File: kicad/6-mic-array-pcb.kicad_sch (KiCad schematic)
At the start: 11 parts, among them J1 USB-C-16P, U1 SF32LB52JUD6, U2 ADAU1977, U3 XC6206P332MR, U4 XC6206P332MR

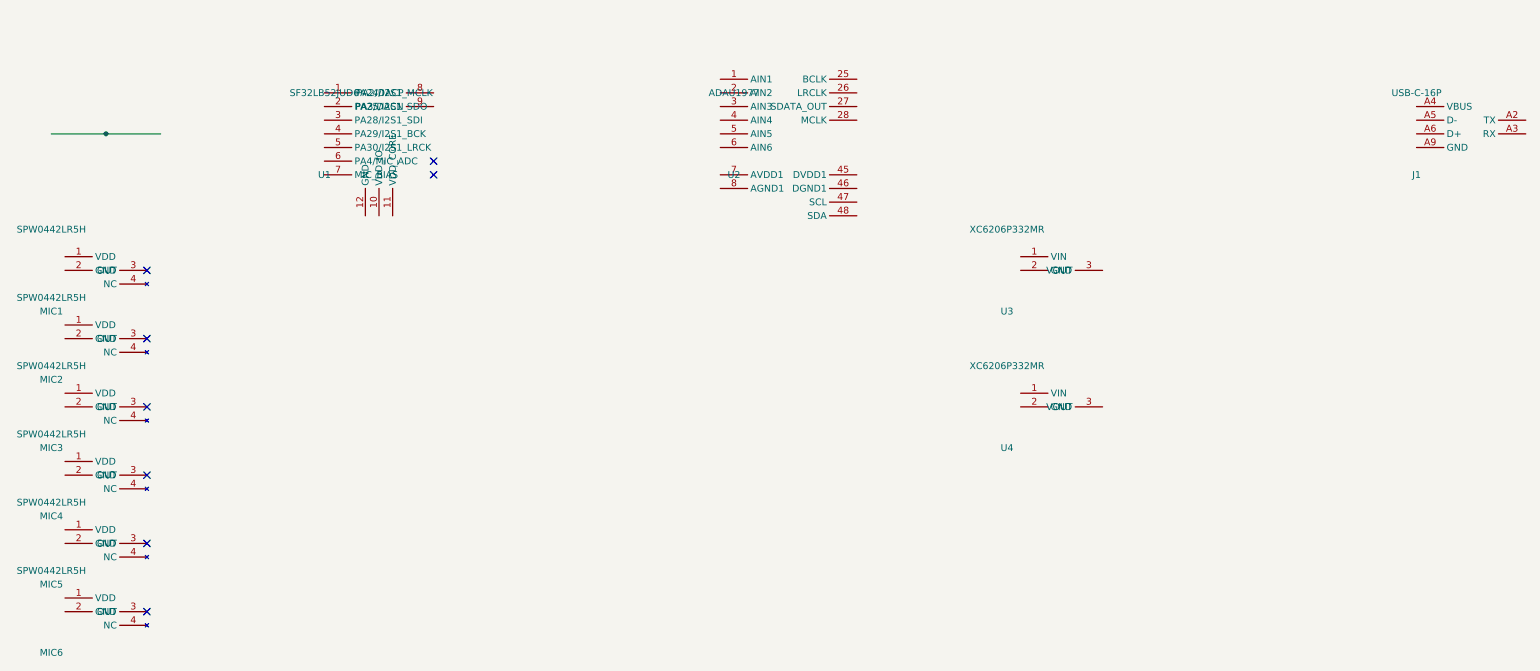
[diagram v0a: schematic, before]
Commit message: feat(common): add pdf
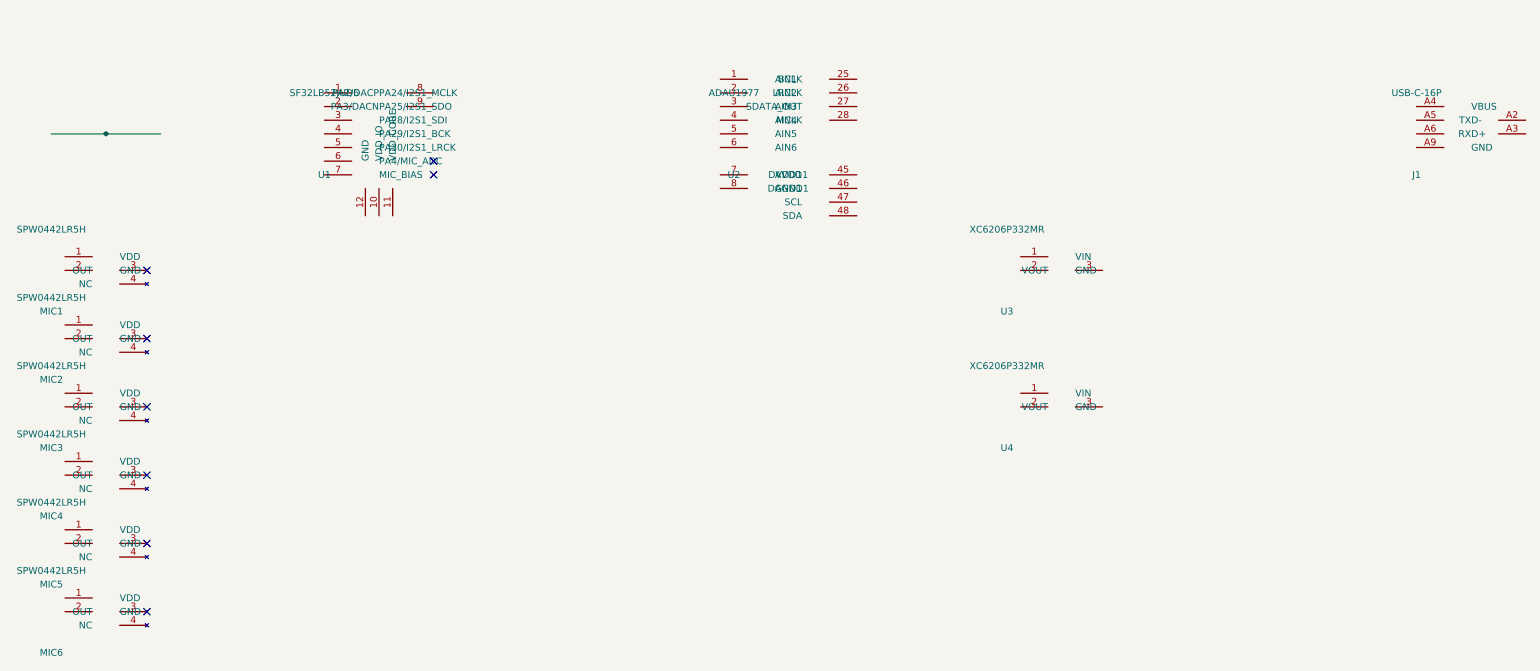
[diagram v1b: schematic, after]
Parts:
- J1: footprint Connector_USB:USB_C_Receptacle_PCB -> Connector_USB:USB_C_Receptacle_Amphenol_12401548E4-2A
- MIC1, MIC2, MIC3, MIC4, MIC5, MIC6: footprint Microphone:MEMS_Mic_SMD_4.72x3.76mm -> Sensor_Audio:Knowles_LGA-6_4.72x3.76mm
- U1: footprint Package_LGA:LGA-56_6x6mm_P0.65mm -> 6-mic-array:SF32LB52JUD6_LGA56
- U3, U4: footprint Package_TO_SOT_SMD:SOT-23 -> Package_TO_SOT_SMD:SOT-23-3

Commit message: feat(common): add pdf
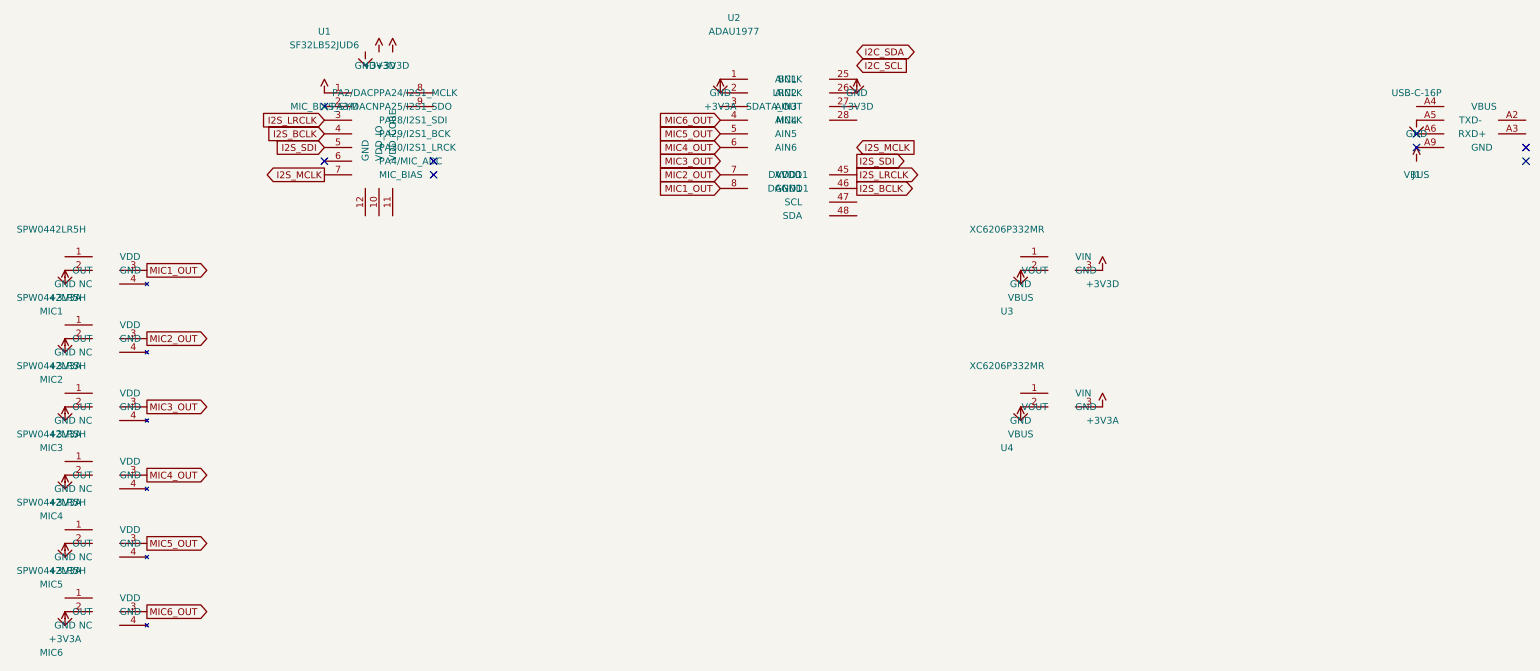
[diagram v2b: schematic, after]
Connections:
- net MIC_BIAS_SYM: now reaches U1.1 (PA24/I2S1_MCLK)
- net I2S_LRCLK: now reaches U1.3 (PA28/I2S1_SDI)
- net I2S_LRCLK: now also U2.45 (DVDD1)
- net I2S_BCLK: now reaches U1.4 (PA29/I2S1_BCK)
- net I2S_BCLK: now also U2.46 (DGND1)
- net I2S_SDI: now reaches U1.5 (PA30/I2S1_LRCK)
- net I2S_MCLK: now reaches U1.7 (MIC_BIAS)
- net GND: now reaches U2.1 (AIN1)
- net GND: now also J1.A5 (D-), MIC1.2 (GND), MIC2.2 (GND), MIC3.2 (GND), MIC4.2 (GND), MIC5.2 (GND), MIC6.2 (GND), U2.25 (BCLK), U3.2 (GND), U4.2 (GND)
- net +3V3A: now reaches U2.2 (AIN2)
- net +3V3A: now also U4.3 (VOUT)
- net +3V3D: now reaches U2.26 (LRCLK)
- net +3V3D: now also U3.3 (VOUT)
- net MIC6_OUT: now reaches U2.4 (AIN4)
- net MIC6_OUT: now also MIC6.3 (OUT)
- net MIC5_OUT: now reaches U2.5 (AIN5)
- net MIC5_OUT: now also MIC5.3 (OUT)
- net MIC4_OUT: now reaches U2.6 (AIN6)
- net MIC4_OUT: now also MIC4.3 (OUT)
- net MIC2_OUT: now reaches U2.7 (AVDD1)
- net MIC2_OUT: now also MIC2.3 (OUT)
- net MIC1_OUT: now reaches U2.8 (AGND1)
- net MIC1_OUT: now also MIC1.3 (OUT)
- net MIC3_OUT: now reaches MIC3.3 (OUT)
